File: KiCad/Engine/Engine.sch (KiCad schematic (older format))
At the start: 4 parts, among them J2 Power, J6 P1, J7 P2, J8 Move

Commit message: Engine ready for validation+layout
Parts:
- removed J2: Power, Connector_PinHeader_1.27mm:PinHeader_2x05_P1.27mm_Vertical, symbol Connector_Generic:Conn_02x05_Odd_Even
- removed J6: P1, Connector_PinHeader_1.27mm:PinHeader_2x05_P1.27mm_Vertical, symbol Connector_Generic:Conn_01x10
- removed J7: P2, Connector_PinHeader_1.27mm:PinHeader_2x05_P1.27mm_Vertical, symbol Connector_Generic:Conn_01x10
- removed J8: Move, Connector_PinHeader_1.27mm:PinHeader_2x05_P1.27mm_Vertical, symbol Connector_Generic:Conn_01x10
- added H1, H2: MountingHole, MountingHole:MountingHole_3.2mm_M3_Pad_Via, symbol Mechanical:MountingHole
- added J1: Power, Connector_PinSocket_2.54mm:PinSocket_1x10_P2.54mm_Horizontal, symbol Connector_Generic:Conn_01x10
- added J3: P1, Connector_PinSocket_2.54mm:PinSocket_1x10_P2.54mm_Horizontal, symbol Connector_Generic:Conn_01x10
- added J4: P2, Connector_PinSocket_2.54mm:PinSocket_1x10_P2.54mm_Horizontal, symbol Connector_Generic:Conn_01x10
- added J5: Move, Connector_PinSocket_2.54mm:PinSocket_1x10_P2.54mm_Horizontal, symbol Connector_Generic:Conn_01x10
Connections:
- wire segments 211 -> 237

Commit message: Changed to female connectors
    Layout finished, still need to do via-in-pad/silk checks
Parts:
- J1, J3, J4, J5: footprint Connector_PinSocket_2.54mm:PinSocket_1x10_P2.54mm_Horizontal -> Connector_PinHeader_2.54mm:PinHeader_1x10_P2.54mm_Vertical
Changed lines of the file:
@@
 F 0 "J3" V 8017 10096 50  0000 C CNN
 F 1 "P1" V 7926 10096 50  0000 C CNN
-F 2 "Connector_PinSocket_2.54mm:PinSocket_1x10_P2.54mm_Horizontal" H 7800 10150 50  0001 C CNN
+F 2 "Connector_PinHeader_2.54mm:PinHeader_1x10_P2.54mm_Vertical" H 7800 10150 50  0001 C CNN
 F 3 "~" H 7800 10150 50  0001 C CNN
 	1    7800 10150
@@
 F 0 "J4" V 9367 10096 50  0000 C CNN
 F 1 "P2" V 9276 10096 50  0000 C CNN
-F 2 "Connector_PinSocket_2.54mm:PinSocket_1x10_P2.54mm_Horizontal" H 9150 10150 50  0001 C CNN
+F 2 "Connector_PinHeader_2.54mm:PinHeader_1x10_P2.54mm_Vertical" H 9150 10150 50  0001 C CNN
 F 3 "~" H 9150 10150 50  0001 C CNN
 	1    9150 10150
@@
 F 0 "J5" V 10717 10096 50  0000 C CNN
 F 1 "Move" V 10626 10096 50  0000 C CNN
-F 2 "Connector_PinSocket_2.54mm:PinSocket_1x10_P2.54mm_Horizontal" H 10500 10150 50  0001 C CNN
+F 2 "Connector_PinHeader_2.54mm:PinHeader_1x10_P2.54mm_Vertical" H 10500 10150 50  0001 C CNN
 F 3 "~" H 10500 10150 50  0001 C CNN
 	1    10500 10150
@@
 F 0 "J1" V 6667 10096 50  0000 C CNN
 F 1 "Power" V 6576 10096 50  0000 C CNN
-F 2 "Connector_PinSocket_2.54mm:PinSocket_1x10_P2.54mm_Horizontal" H 6450 10150 50  0001 C CNN
+F 2 "Connector_PinHeader_2.54mm:PinHeader_1x10_P2.54mm_Vertical" H 6450 10150 50  0001 C CNN
 F 3 "~" H 6450 10150 50  0001 C CNN
 	1    6450 10150

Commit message: Small engine fix
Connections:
- wire segments 237 -> 236
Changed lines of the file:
@@
 	8950 10900 8950 10350
-Wire Wire Line
-	9050 10900 9050 10550
 Wire Wire Line
 	9150 10900 9150 10350
@@
 	7700 10450 7700 10350
 Wire Wire Line
-	9050 10450 9050 10350
+	10400 10350 10400 10900
 Wire Wire Line
-	10400 10350 10400 10900
+	9050 10350 9050 10900
 Wire Bus Line
 	13800 1550 13800 6200

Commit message: Engine Fixes
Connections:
- wire segments 236 -> 237
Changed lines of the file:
@@
 	7600 10900 7600 10350
-Wire Wire Line
-	7700 10900 7700 10550
 Wire Wire Line
 	7800 10900 7800 10350
@@
 Wire Wire Line
 	10100 10350 10100 10900
-Text Label 10200 10900 1    50   ~ 0
+Text Label 11000 10900 1    50   ~ 0
 Computer8
-Text Label 10300 10900 1    50   ~ 0
+Text Label 10900 10900 1    50   ~ 0
 Computer7
-Text Label 10400 10900 1    50   ~ 0
+Text Label 10800 10900 1    50   ~ 0
 Computer6
-Text Label 10500 10900 1    50   ~ 0
+Text Label 10700 10900 1    50   ~ 0
 Computer5
 Text Label 10600 10900 1    50   ~ 0
 Computer4
-Text Label 10700 10900 1    50   ~ 0
+Text Label 10500 10900 1    50   ~ 0
 Computer3
-Text Label 10800 10900 1    50   ~ 0
+Text Label 10400 10900 1    50   ~ 0
 Computer2
-Text Label 10900 10900 1    50   ~ 0
+Text Label 10300 10900 1    50   ~ 0
 Computer1
-Text Label 11000 10900 1    50   ~ 0
+Text Label 10200 10900 1    50   ~ 0
 Computer0
 Wire Wire Line
@@
 	9650 10900 9650 10350
 Wire Wire Line
+	11000 10900 11000 10350
+Wire Wire Line
+	10900 10900 10900 10350
+Wire Wire Line
+	10700 10900 10700 10350
+Wire Wire Line
+	10600 10900 10600 10350
+Wire Wire Line
+	10500 10900 10500 10350
+Wire Wire Line
+	10400 10900 10400 10350
+Wire Wire Line
+	10300 10900 10300 10350
+Wire Wire Line
 	10200 10900 10200 10350
-Wire Wire Line
-	10300 10900 10300 10350
-Wire Wire Line
-	10500 10900 10500 10350
-Wire Wire Line
-	10600 10900 10600 10350
-Wire Wire Line
-	10700 10900 10700 10350
-Wire Wire Line
-	10800 10900 10800 10350
-Wire Wire Line
-	10900 10900 10900 10350
-Wire Wire Line
-	11000 10900 11000 10350
 $Comp
 L Connector_Generic:Conn_01x10 J3
@@
 	6950 10450 6950 10500
 Wire Wire Line
-	7700 10450 7700 10350
-Wire Wire Line
-	10400 10350 10400 10900
+	10800 10350 10800 10900
 Wire Wire Line
 	9050 10350 9050 10900
+$Comp
+L power:PWR_FLAG #FLG0101
+U 1 1 60713304
+P 5950 10450
+F 0 "#FLG0101" H 5950 10525 50  0001 C CNN
+F 1 "PWR_FLAG" H 5750 10600 50  0000 L CNN
+F 2 "" H 5950 10450 50  0001 C CNN
+F 3 "~" H 5950 10450 50  0001 C CNN
+	1    5950 10450
+	0    -1   -1   0
+$EndComp
+$Comp
+L power:PWR_FLAG #FLG0102
+U 1 1 60714033
+P 7050 10450
+F 0 "#FLG0102" H 7050 10525 50  0001 C CNN
+F 1 "PWR_FLAG" H 6900 10600 50  0000 L CNN
+F 2 "" H 7050 10450 50  0001 C CNN
+F 3 "~" H 7050 10450 50  0001 C CNN
+	1    7050 10450
+	0    1    1    0
+$EndComp
+Wire Wire Line
+	5950 10450 6050 10450
+Wire Wire Line
+	7050 10450 6950 10450
+Wire Wire Line
+	7700 10350 7700 10900
 Wire Bus Line
 	13800 1550 13800 6200

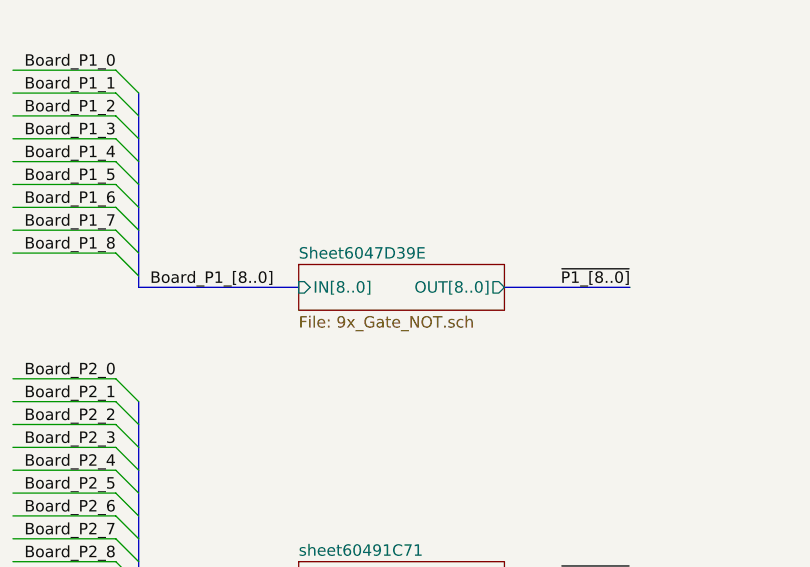
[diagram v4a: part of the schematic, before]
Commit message: Engine: Pre 4in Nor replicate
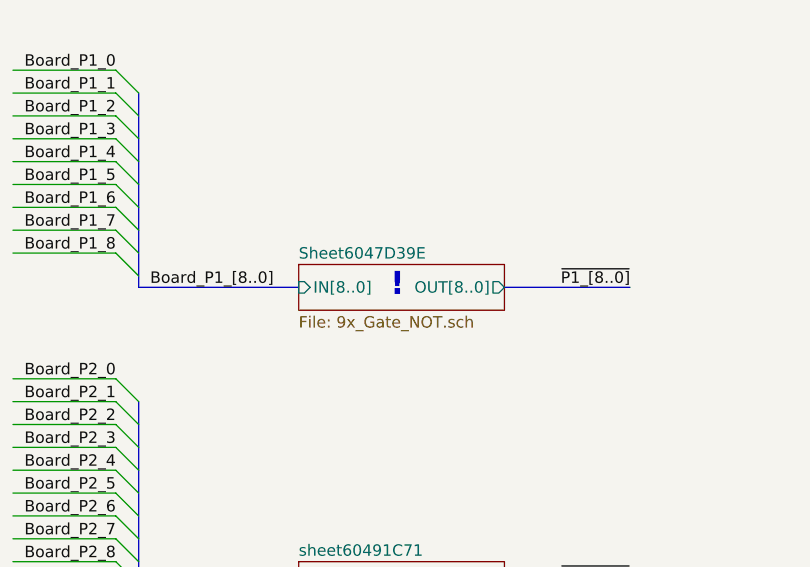
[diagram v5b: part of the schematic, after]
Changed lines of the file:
@@
 Wire Bus Line
 	13800 6200 13800 7300
+Text Notes 3000 9000 0    100  ~ 20
+!
 $EndSCHEMATC

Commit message: Engine layout.
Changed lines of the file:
@@
 F3 "~P2_[8..0]" I L 5100 4850 50
 F4 "~Empty_[8..0]" I L 5100 4950 50
-F5 "Inhib_Out" O R 6100 4550 50
-F6 "Inhib" I L 5100 4550 50
-F7 "M0_K" O R 6100 4750 50
-F8 "M8_K" O R 6100 5050 50
-F9 "M2_K" O R 6100 4850 50
-F10 "M6_K" O R 6100 4950 50
+F5 "M0_K" O R 6100 4750 50
+F6 "M8_K" O R 6100 5050 50
+F7 "M2_K" O R 6100 4850 50
+F8 "M6_K" O R 6100 4950 50
+F9 "Block" I L 5100 4550 50
+F10 "Block_Out" O R 6100 4550 50
 $EndSheet
 Text Label 12200 2600 0    50   ~ 0
@@
 F3 "~P2_[8..0]" I L 7400 4850 50
 F4 "~Empty_[8..0]" I L 7400 4950 50
-F5 "Inhib_Out" O R 8400 4550 50
-F6 "Inhib" I L 7400 4550 50
-F7 "M0_L" O R 8400 4700 50
-F8 "M8_L" O R 8400 5000 50
-F9 "M2_L" O R 8400 4800 50
-F10 "M6_L" O R 8400 4900 50
-$EndSheet
-$Sheet
-S 2800 6100 1000 1200
-U 607BECCD
-F0 "sheet607BECBB" 50
-F1 "Engine_EMPTY_SIDES.sch" 50
-F2 "~P1_[8..0]" I L 2800 6400 50
-F3 "~P2_[8..0]" I L 2800 6500 50
-F4 "~Empty_[8..0]" I L 2800 6600 50
-F5 "Inhib" I L 2800 6200 50
-F6 "M1_M" O R 3800 6400 50
-F7 "M3_M" O R 3800 6500 50
-F8 "M7_M" O R 3800 6700 50
-F9 "M5_M" O R 3800 6600 50
+F5 "M0_L" O R 8400 4700 50
+F6 "M8_L" O R 8400 5000 50
+F7 "M2_L" O R 8400 4800 50
+F8 "M6_L" O R 8400 4900 50
+F9 "Block" I L 7400 4550 50
+F10 "Block_Out" O R 8400 4550 50
 $EndSheet
 Wire Wire Line
@@
 F3 "~P2_[8..0]" I L 2800 4850 50
 F4 "~Empty_[8..0]" I L 2800 4950 50
-F5 "Inhib_Out" O R 3800 4550 50
-F6 "Inhib" I L 2800 4550 50
-F7 "M7_I" O R 3800 4850 50
-F8 "M4_I" O R 3800 4750 50
-F9 "M8_I" O R 3800 4950 50
-F10 "M7_J" O R 3800 5150 50
+F5 "M7_I" O R 3800 4850 50
+F6 "M4_I" O R 3800 4750 50
+F7 "M8_I" O R 3800 4950 50
+F8 "M7_J" O R 3800 5150 50
+F9 "Block" I L 2800 4550 50
+F10 "Block_Out" O R 3800 4550 50
 $EndSheet
 Wire Bus Line
@@
 F3 "~P2_[8..0]" I L 7400 3200 50
 F4 "~Empty_[8..0]" I L 7400 3300 50
-F5 "Inhib_Out" O R 8400 2900 50
-F6 "Inhib" I L 7400 2900 50
-F7 "M0_G" O R 8400 3100 50
-F8 "M4_G" O R 8400 3200 50
-F9 "M8_G" O R 8400 3300 50
-F10 "M2_H" O R 8400 3500 50
-F11 "M4_H" O R 8400 3600 50
-F12 "M6_H" O R 8400 3700 50
+F5 "M0_G" O R 8400 3100 50
+F6 "M4_G" O R 8400 3200 50
+F7 "M8_G" O R 8400 3300 50
+F8 "M2_H" O R 8400 3500 50
+F9 "M4_H" O R 8400 3600 50
+F10 "M6_H" O R 8400 3700 50
+F11 "Block_Out" O R 8400 2900 50
+F12 "Block" I L 7400 2900 50
 $EndSheet
 Wire Wire Line
@@
 F3 "~P2_[8..0]" I L 5100 3200 50
 F4 "~Empty_[8..0]" I L 5100 3300 50
-F5 "Inhib_Out" O R 6100 2900 50
-F6 "Inhib" I L 5100 2900 50
-F7 "M0_F" O R 6100 3100 50
-F8 "M1_F" O R 6100 3200 50
-F9 "M2_F" O R 6100 3300 50
-F10 "M5_F" O R 6100 3600 50
-F11 "M6_F" O R 6100 3700 50
-F12 "M7_F" O R 6100 3800 50
-F13 "M8_F" O R 6100 3900 50
-F14 "M4_F" O R 6100 3500 50
-F15 "M3_F" O R 6100 3400 50
+F5 "M0_F" O R 6100 3100 50
+F6 "M1_F" O R 6100 3200 50
+F7 "M2_F" O R 6100 3300 50
+F8 "M5_F" O R 6100 3600 50
+F9 "M6_F" O R 6100 3700 50
+F10 "M7_F" O R 6100 3800 50
+F11 "M8_F" O R 6100 3900 50
+F12 "M4_F" O R 6100 3500 50
+F13 "M3_F" O R 6100 3400 50
+F14 "Block_Out" O R 6100 2900 50
+F15 "Block" I L 5100 2900 50
 $EndSheet
 Wire Bus Line
@@
 F3 "~P2_[8..0]" I L 2800 3200 50
 F4 "~Empty_[8..0]" I L 2800 3300 50
-F5 "Inhib_Out" O R 3800 2900 50
-F6 "Inhib" I L 2800 2900 50
-F7 "M0_E" O R 3800 3100 50
-F8 "M1_E" O R 3800 3200 50
-F9 "M2_E" O R 3800 3300 50
-F10 "M3_E" O R 3800 3400 50
-F11 "M4_E" O R 3800 3500 50
-F12 "M5_E" O R 3800 3600 50
-F13 "M6_E" O R 3800 3700 50
-F14 "M7_E" O R 3800 3800 50
-F15 "M8_E" O R 3800 3900 50
+F5 "M0_E" O R 3800 3100 50
+F6 "M1_E" O R 3800 3200 50
+F7 "M2_E" O R 3800 3300 50
+F8 "M3_E" O R 3800 3400 50
+F9 "M4_E" O R 3800 3500 50
+F10 "M5_E" O R 3800 3600 50
+F11 "M6_E" O R 3800 3700 50
+F12 "M7_E" O R 3800 3800 50
+F13 "M8_E" O R 3800 3900 50
+F14 "Block_Out" O R 3800 2900 50
+F15 "Block" I L 2800 2900 50
 $EndSheet
 Wire Bus Line
@@
 F3 "~P2_[8..0]" I L 7400 1550 50
 F4 "~Empty_[8..0]" I L 7400 1650 50
-F5 "Inhib_Out" O R 8400 1250 50
-F6 "Inhib" I L 7400 1250 50
-F7 "M0_C" O R 8400 1450 50
-F8 "M4_C" O R 8400 1550 50
-F9 "M8_C" O R 8400 1650 50
-F10 "M2_D" O R 8400 1850 50
-F11 "M4_D" O R 8400 1950 50
-F12 "M6_D" O R 8400 2050 50
+F5 "M0_C" O R 8400 1450 50
+F6 "M4_C" O R 8400 1550 50
+F7 "M8_C" O R 8400 1650 50
+F8 "M2_D" O R 8400 1850 50
+F9 "M4_D" O R 8400 1950 50
+F10 "M6_D" O R 8400 2050 50
+F11 "Block_Out" O R 8400 1250 50
+F12 "Block" I L 7400 1250 50
 $EndSheet
 Wire Bus Line
@@
 F3 "~P2_[8..0]" I L 5100 1550 50
 F4 "~Empty_[8..0]" I L 5100 1650 50
-F5 "Inhib_Out" O R 6100 1250 50
-F6 "Inhib" I L 5100 1250 50
-F7 "M0_B" O R 6100 1450 50
-F8 "M1_B" O R 6100 1550 50
-F9 "M2_B" O R 6100 1650 50
-F10 "M3_B" O R 6100 1750 50
-F11 "M4_B" O R 6100 1850 50
-F12 "M5_B" O R 6100 1950 50
-F13 "M6_B" O R 6100 2050 50
-F14 "M7_B" O R 6100 2150 50
-F15 "M8_B" O R 6100 2250 50
+F5 "M0_B" O R 6100 1450 50
+F6 "M1_B" O R 6100 1550 50
+F7 "M2_B" O R 6100 1650 50
+F8 "M3_B" O R 6100 1750 50
+F9 "M4_B" O R 6100 1850 50
+F10 "M5_B" O R 6100 1950 50
+F11 "M6_B" O R 6100 2050 50
+F12 "M7_B" O R 6100 2150 50
+F13 "M8_B" O R 6100 2250 50
+F14 "Block_Out" O R 6100 1250 50
+F15 "Block" I L 5100 1250 50
 $EndSheet
 $Sheet
@@
 F12 "M8_A" O R 3800 2250 50
 F13 "~Empty_[8..0]" I L 2800 1650 50
-F14 "Inhib_Out" O R 3800 1250 50
+F14 "Block_Out" O R 3800 1250 50
 $EndSheet
 Entry Wire Line
@@
 Wire Wire Line
 	7700 10350 7700 10900
-Wire Bus Line
-	13800 1550 13800 6200
-Wire Bus Line
-	12050 1650 12050 6200
-Wire Bus Line
-	1900 9450 1900 10250
-Wire Bus Line
-	1900 8100 1900 8950
-Wire Bus Line
-	13800 6200 13800 7300
 Text Notes 3000 9000 0    100  ~ 20
 !
+Wire Bus Line
+	13800 6200 13800 7300
+Wire Bus Line
+	12050 1650 12050 6200
+Wire Bus Line
+	13800 1550 13800 6200
+Wire Bus Line
+	1900 9450 1900 10250
+Wire Bus Line
+	1900 8100 1900 8950
+$Sheet
+S 2800 6100 1000 1200
+U 607BECCD
+F0 "sheet607BECBB" 50
+F1 "Engine_EMPTY_SIDES.sch" 50
+F2 "~P1_[8..0]" I L 2800 6400 50
+F3 "~P2_[8..0]" I L 2800 6500 50
+F4 "~Empty_[8..0]" I L 2800 6600 50
+F5 "M1_M" O R 3800 6400 50
+F6 "M3_M" O R 3800 6500 50
+F7 "M7_M" O R 3800 6700 50
+F8 "M5_M" O R 3800 6600 50
+F9 "Block" I L 2800 6200 50
+$EndSheet
 $EndSCHEMATC
